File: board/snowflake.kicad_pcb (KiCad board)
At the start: 2 copper layers, 129 x 148.8 mm, 82 parts, among them J1 Conn_01x02_Pin, J3 TC2030, U1 TZ-5050S2RGB-5V-I4-H1, U10 TZ-5050S2RGB-5V-I4-H1, U11 TZ-5050S2RGB-5V-I4-H1, U12 TZ-5050S2RGB-5V-I4-H1, U13 TZ-5050S2RGB-5V-I4-H1, U14 TZ-5050S2RGB-5V-I4-H1, U15 TZ-5050S2RGB-5V-I4-H1, U16 TZ-5050S2RGB-5V-I4-H1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

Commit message: Final board updates before sending
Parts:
- removed R0: 510k, Resistor_SMD:R_0603_1608Metric
- added REF**: Next, snowflake:Next, F.Cu at (129.5, 139.2)
- added REF**: Shuffle, snowflake:Shuffle, F.Cu at (129.6, 145.1)
- added REF**: Brightness, snowflake:Brightness, F.Cu at (129.5, 151.0)
- C66: footprint snowflake:C_0402_1005Metric -> Capacitor_SMD:C_0603_1608Metric
- R1: value 220k -> 732k
- TP5, TP6, TP7: footprint snowflake:TestPoint_Pad_D2.0mm -> snowflake:TouchPad
- moved R7 35.6 mm to (127.9, 136.3), turned to 0 degrees
- moved TP7 32.4 mm to (129.5, 139.2)
- moved R6 29.2 mm to (128.0, 142.1), turned to 0 degrees
- moved TP6 28.0 mm to (129.5, 145.1)
- moved TP5 24.0 mm to (129.5, 151.0)
- moved R5 20.2 mm to (128.0, 148.1), turned to 0 degrees
- moved S1 13.7 mm to (160.9, 170.7)
- moved R2 10.2 mm to (153.3, 173.2)
- moved R1 9.95 mm to (152.0, 173.2)
- moved C25 9.00 mm to (150.1, 175.9)
- moved C26 9.00 mm to (150.1, 177.4)
- moved C27 9.00 mm to (148.8, 170.7)
- moved L1 9.00 mm to (146.2, 171.7)
- moved U25 9.00 mm to (150.1, 173.5)
- moved REF** 5.15 mm to (151.9, 146.9)
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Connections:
- R1 pad 1: Net-(R0-Pad1) -> /FB
- S1 pad 1: GND -> /BAT+
- S1 pad 3: /BAT+ -> GND
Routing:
- net /TOUCH3: track 54.8 -> 27.8 mm
- net /TOUCH2: track 47.3 -> 22.1 mm
- net /TOUCH1: track 35.8 -> 14.4 mm
- net /BAT+: track 44.3 -> 55.5 mm
- net /EN: track 14.7 -> 11.7 mm
- net Net-(R0-Pad1): track 1.49 -> 0.00 mm
- net /DIN: track 22.0 -> 23.2 mm
- net /FB: track 2.06 -> 1.21 mm
- net /SWIO: track 11.3 -> 10.7 mm
- net /RX: track 15.3 -> 14.8 mm
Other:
- board text added: "May your holiday be as bright as a starlit night."
- board text added: "Terrance, Ky, & Portabella 2025"

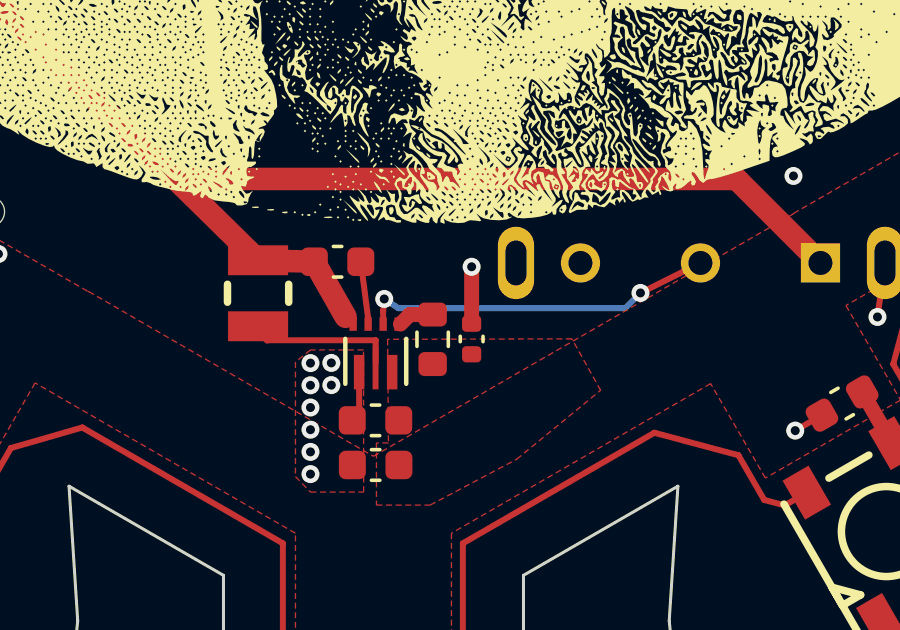
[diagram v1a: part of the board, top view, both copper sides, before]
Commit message: Catch what would have been a huge mistake
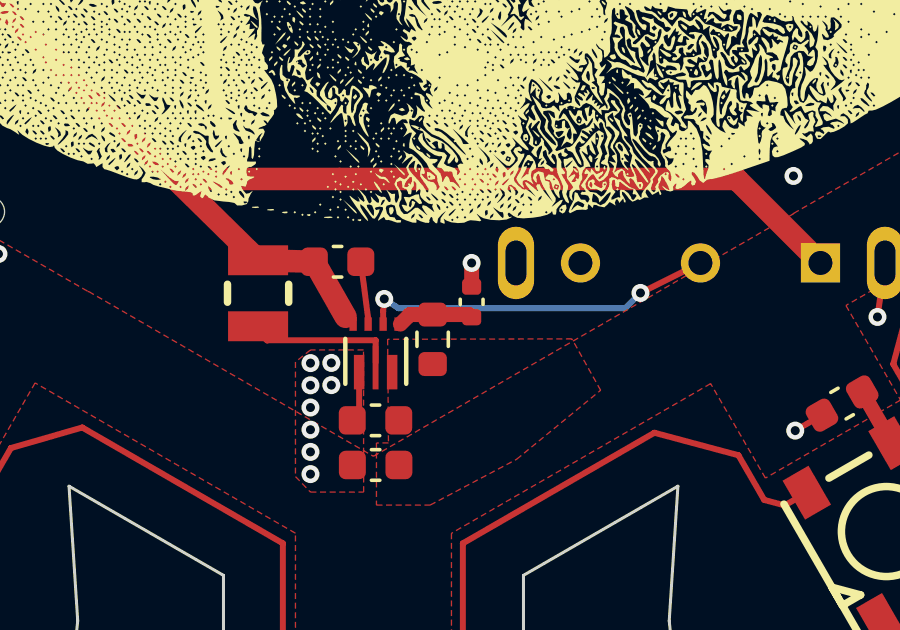
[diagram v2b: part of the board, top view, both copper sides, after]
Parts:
- moved R2 1.23 mm to (153.3, 172.0)
- turned R1 to 90 degrees
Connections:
- R1 pad 1: /FB -> Vdd
- R1 pad 2: Vdd -> /FB
- R2 pad 1: Vdd -> /FB
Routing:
- net /FB: track 1.21 -> 2.54 mm
- net GND: track 68.9 -> 67.8 mm

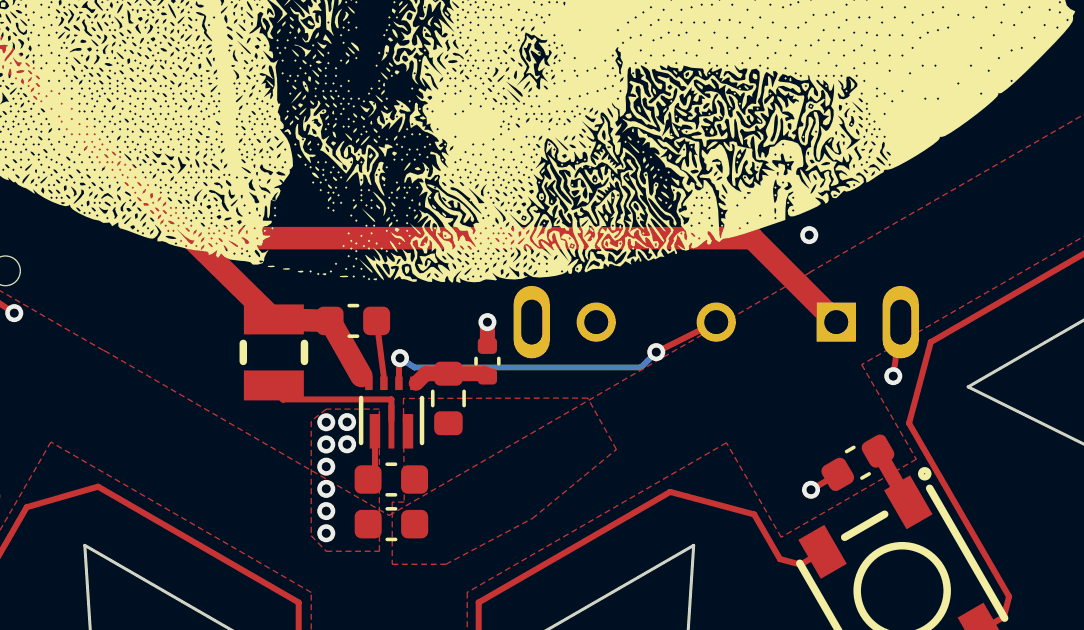
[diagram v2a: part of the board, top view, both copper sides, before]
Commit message: Cleanup power switch traces
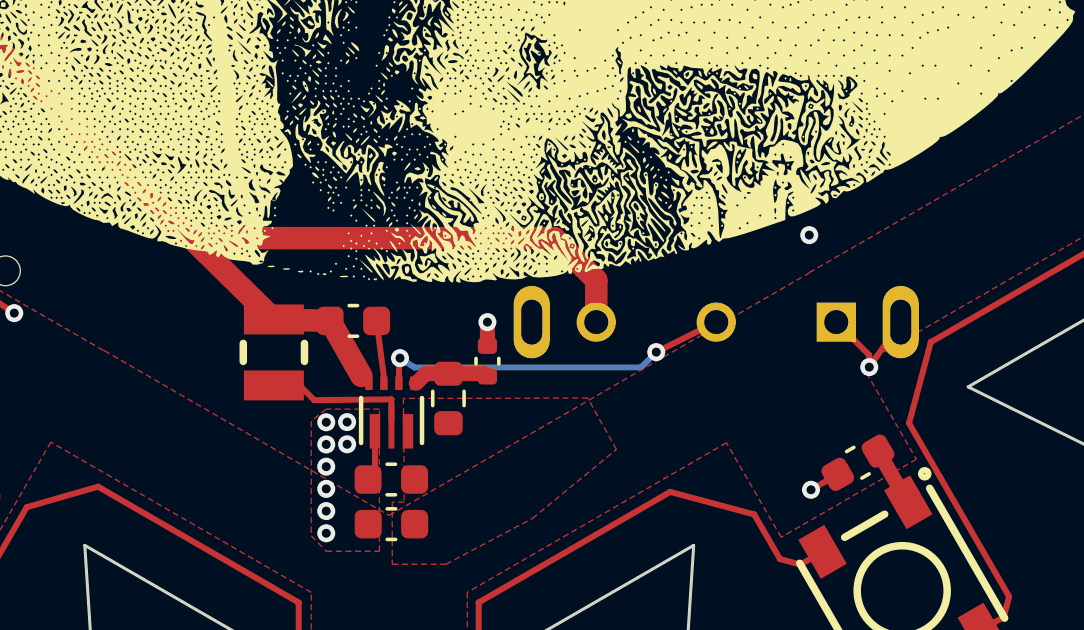
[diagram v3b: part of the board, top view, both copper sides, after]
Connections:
- S1 pad 1: /BAT+ -> GND
- S1 pad 3: GND -> /BAT+
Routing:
- net /BAT+: track 55.5 -> 48.3 mm
- net GND: track 67.8 -> 69.8 mm
